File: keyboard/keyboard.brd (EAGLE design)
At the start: 113 x 131.5 mm, 39 parts, among them SW1 CHERRY_MX, SW10 CHERRY_MX, SW11 CHERRY_MX, SW12 CHERRY_MX, SW13 CHERRY_MX, SW14 CHERRY_MX, SW15 CHERRY_MX, SW16 CHERRY_MX, SW17 CHERRY_MX, SW18 CHERRY_MX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

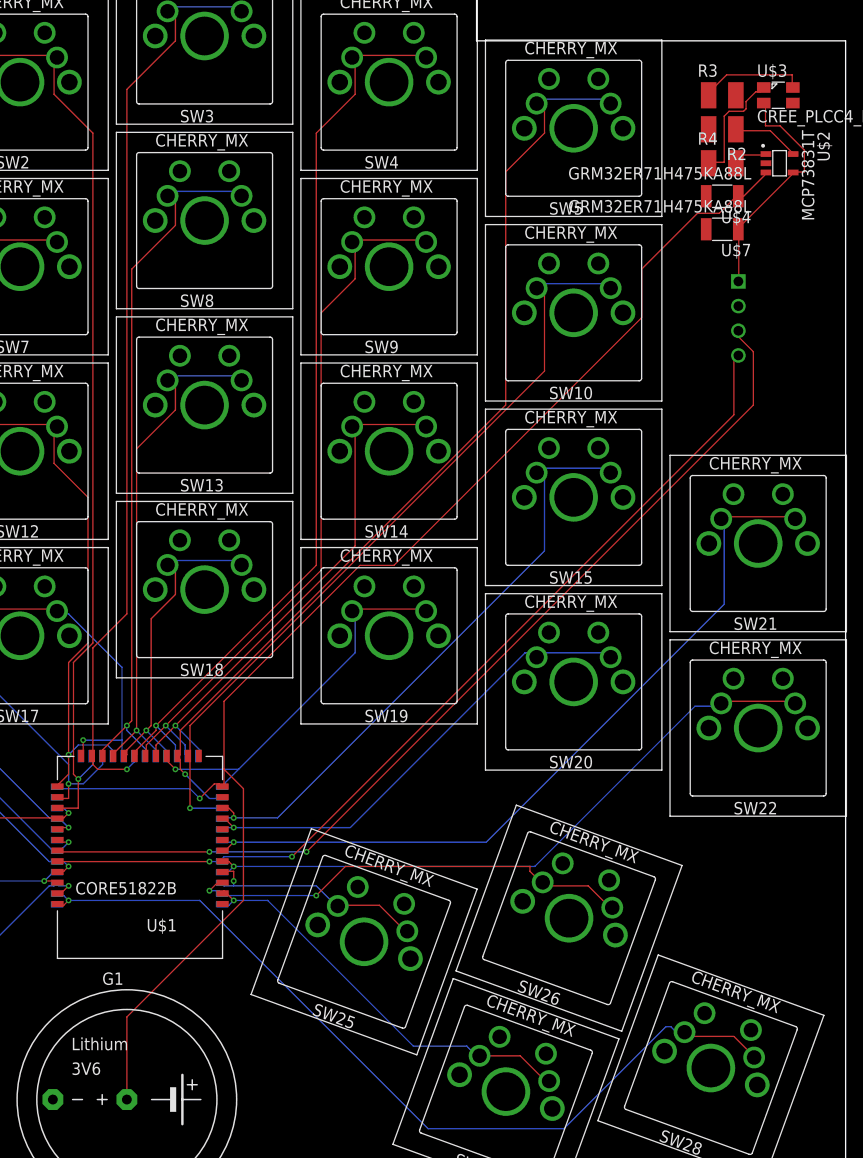
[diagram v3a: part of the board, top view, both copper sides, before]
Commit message: mirror charging circuit on board bottom
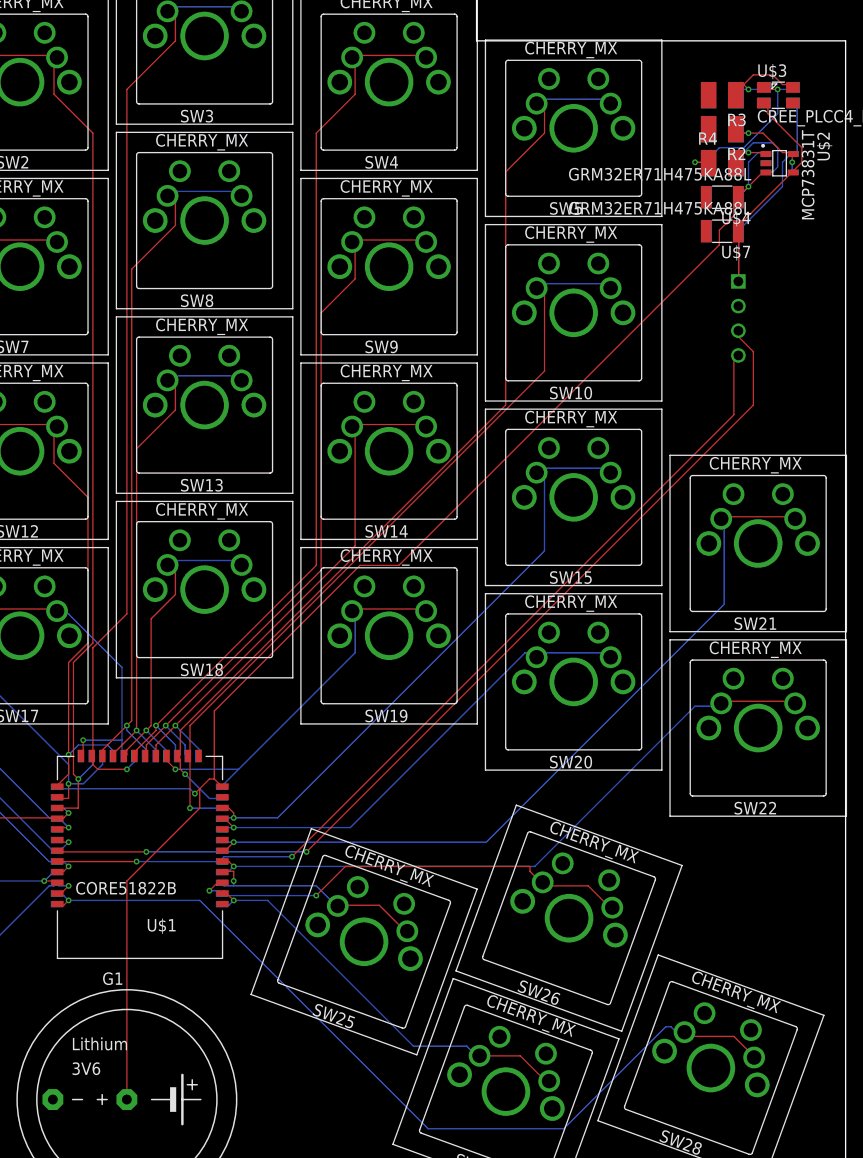
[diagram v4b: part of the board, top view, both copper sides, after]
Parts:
- added R1, R5, R6: 2k, resistor:R1210
- added U$10, U$11: GRM32ER71H475KA88L, GRM32ER71H475KA88L:GRM32ER71H475KA88L
- added U$8: CREE_PLCC4_RGB_LED, cree_plcc4_rgb_led:4-PLCC
- added U$9: MCP73831T, mcp73831t:MCP73831T
- moved U$7 0.20 mm to (100.3, 102.4)
- moved U$4 0.10 mm to (100.3, 105.9)
- turned R3 to 180 degrees
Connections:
- net GND: now also R1.2, R5.2, U$10.P$2, U$11.P$2, U$9.2-VSS
- net GREEN: now also R5.1, U$8.GREEN
- net PROG: now also R1.1, U$9.5-PROG
- net RED: now also R6.1, U$8.RED
- net RSINK: now also R6.2, U$9.1-STAT
- net VCC: now also U$10.P$1, U$9.3-VBAT
- net VIN: now also U$11.P$1, U$8.ANODE, U$9.4VDD
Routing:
- net VIN: track 24.4 -> 45.1 mm
- net RSINK: track 3.53 -> 13.6 mm, vias 0 -> 1
- net RED: track 12.2 -> 18.1 mm, vias 0 -> 2
- net PROG: track 7.02 -> 10.6 mm, vias 0 -> 2
- net GREEN: track 11.1 -> 12.1 mm, vias 0 -> 1
- net VCC: vias 1 -> 2

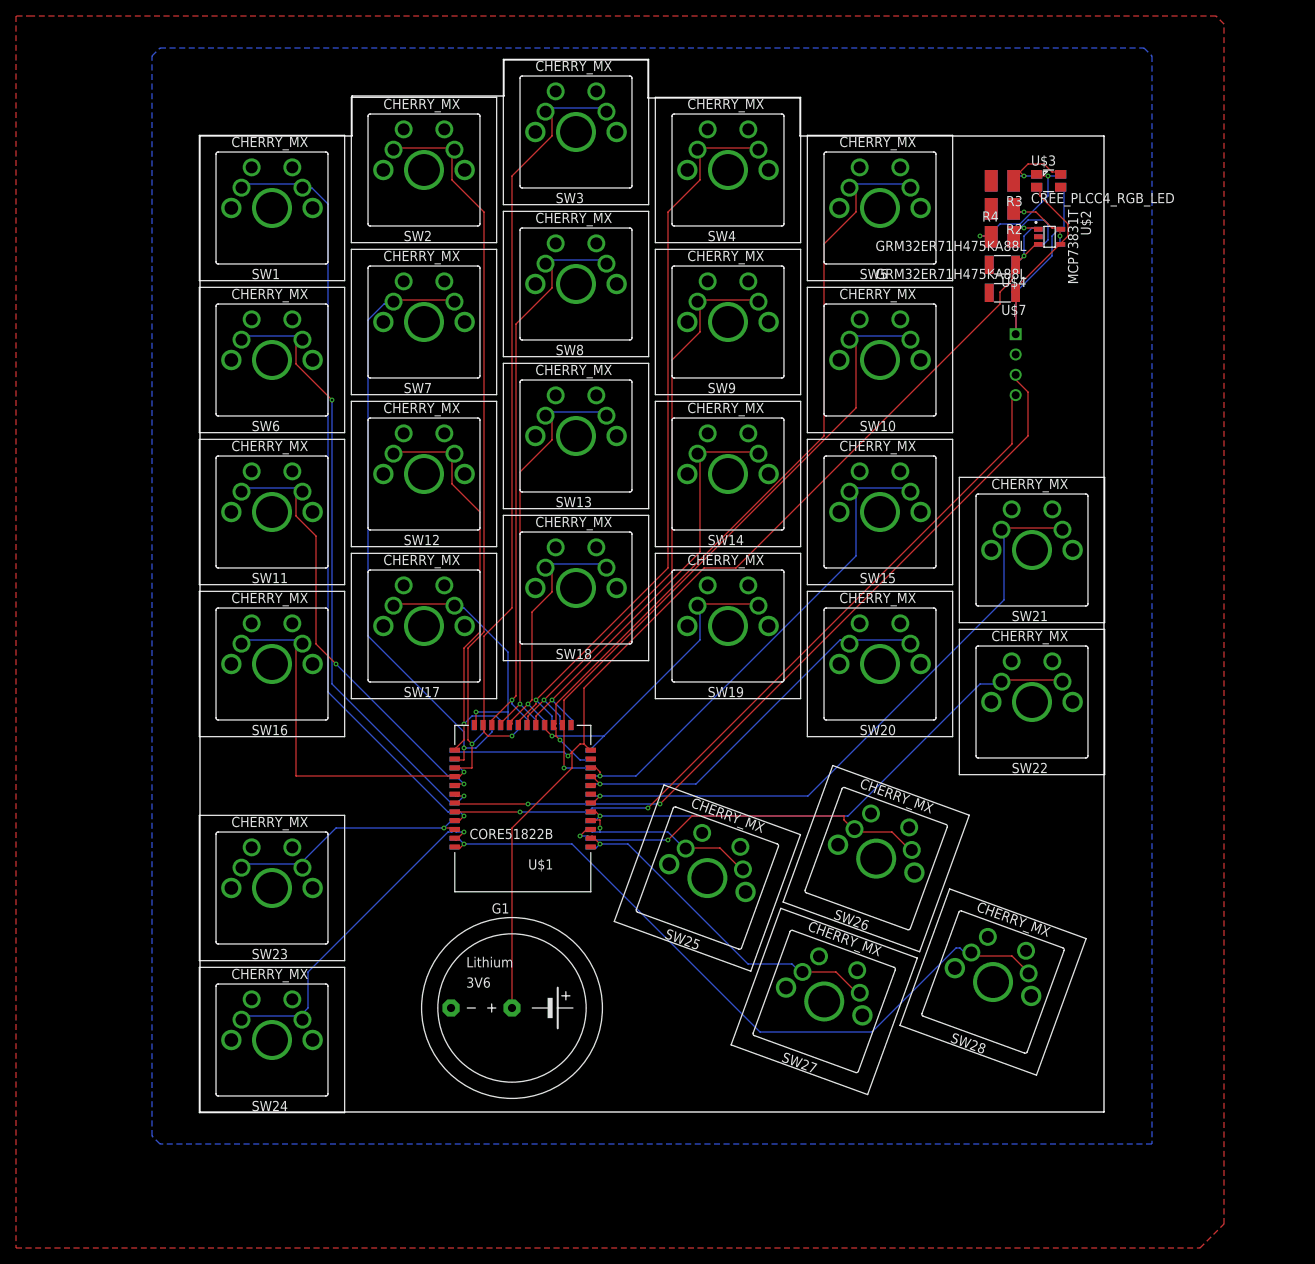
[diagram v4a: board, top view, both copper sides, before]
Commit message: smash labels and values
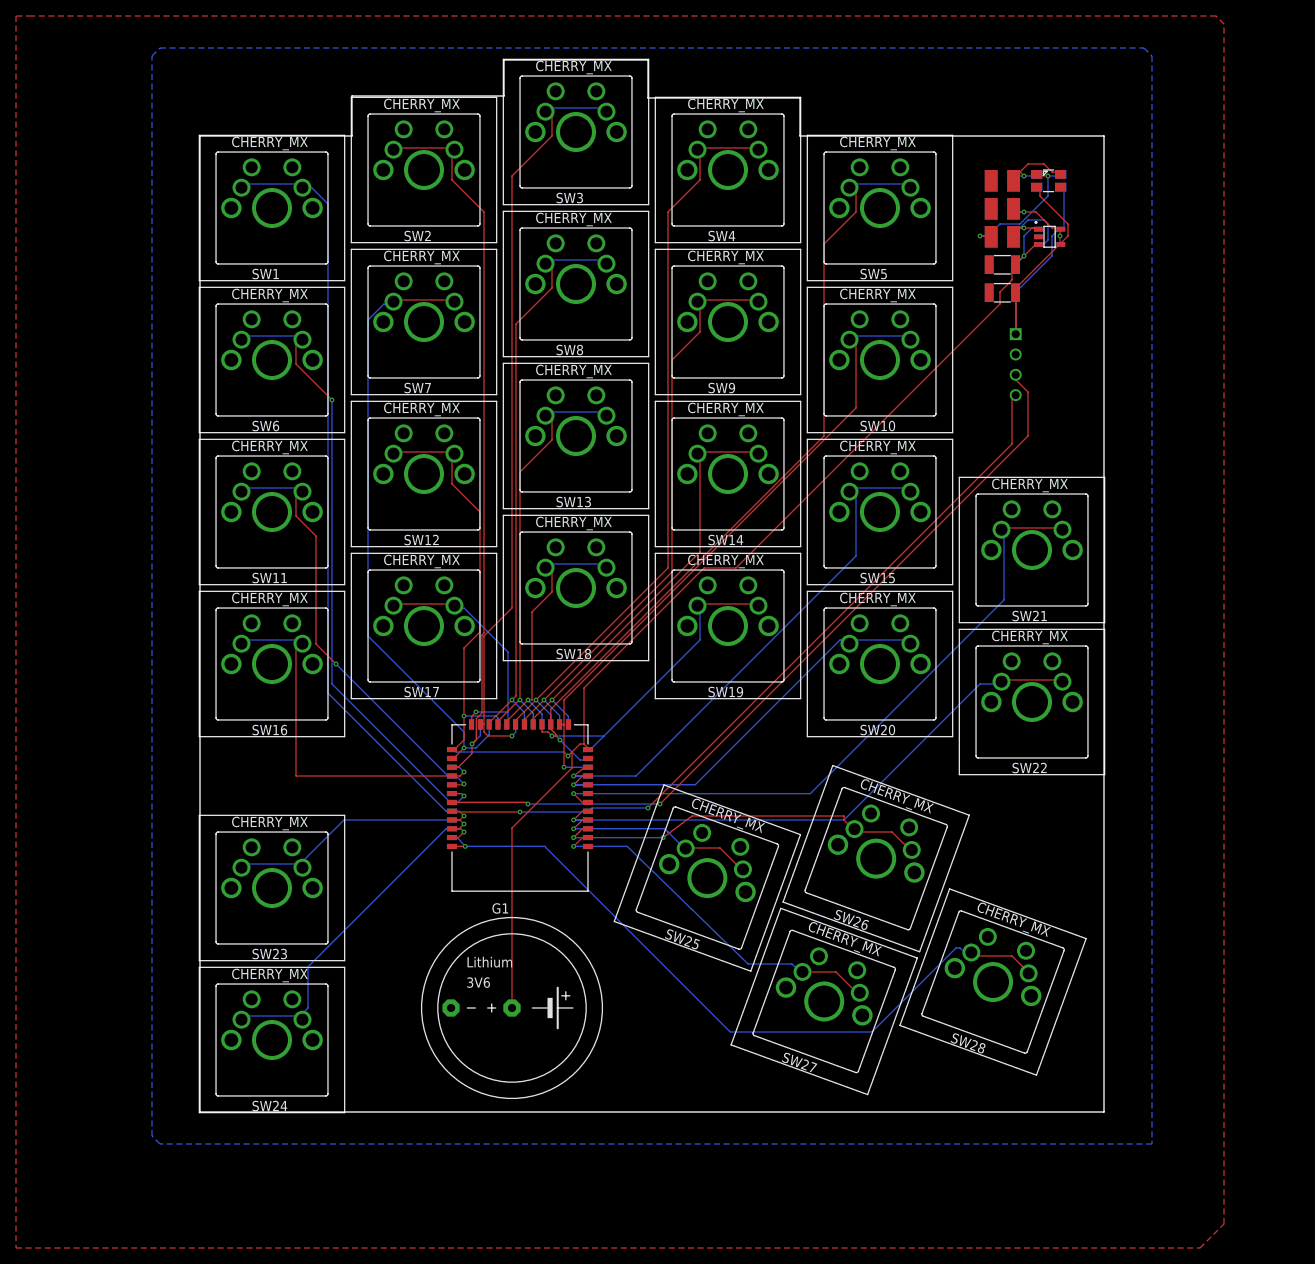
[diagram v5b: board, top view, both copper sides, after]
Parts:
- moved U$1 0.36 mm to (40.0, 38.0)
- moved U$6 0.32 mm to (40.0, 38.0)
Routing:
- net SW20: track 49.9 -> 55.0 mm
- net SW22: track 67.7 -> 72.5 mm
- net SW15: track 63.1 -> 67.8 mm
- net SW21: track 80.2 -> 83.3 mm
- net SW27: track 43.3 -> 45.5 mm
- net SW23: track 31.1 -> 32.9 mm
- net SW25: track 23.8 -> 25.6 mm
- net SW2: track 93.0 -> 91.7 mm
- net SW26: track 46.8 -> 47.8 mm
- net SW18: track 34.0 -> 34.8 mm
- net SW19: track 39.9 -> 40.7 mm
- net SW7: track 78.3 -> 77.6 mm
- net SW28: track 89.5 -> 90.1 mm
- net SWDIO: track 99.1 -> 99.7 mm
- net SW13: track 53.5 -> 54.0 mm
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
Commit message: reroute
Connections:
- new net SW29: U$1.P10, U$6.P30
- net SW10: now also U$1.P30, U$6.P10; no longer U$1.P00, U$6.P13
- net SW12: now also U$6.P13; no longer U$6.P02
- net SW13: now also U$1.P06, U$6.P03; no longer U$1.P07, U$6.P06
- net SW14: now also U$1.P02, U$6.P07; no longer U$1.P03, U$6.P10
- net SW17: now also U$1.P09, U$6.P00; no longer U$1.P10, U$6.P03
- net SW18: now also U$1.P05, U$6.P04; no longer U$1.P06, U$6.P07
- net SW19: now also U$1.P01, U$6.P08; no longer U$1.P02, U$6.P11
- net SW2: now also U$6.P11; no longer U$6.P00
- net SW3: now also U$1.P08, U$6.P01; no longer U$1.P09, U$6.P04
- net SW4: now also U$1.P04, U$6.P05; no longer U$1.P05, U$6.P08
- net SW5: now also U$1.P00, U$6.P09; no longer U$1.P01, U$6.P12
- net SW7: now also U$6.P12; no longer U$6.P01
- net SW8: now also U$1.P07, U$6.P02; no longer U$1.P08, U$6.P05
- net SW9: now also U$1.P03, U$6.P06; no longer U$1.P04, U$6.P09
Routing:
- net SWDIO: track 99.7 -> 214.6 mm, vias 2 -> 3
- net VCC: track 148.3 -> 243.2 mm
- net SW10: track 80.7 -> 128.9 mm, vias 1 -> 2
- net SW15: track 67.8 -> 108.1 mm
- net SW2: track 91.7 -> 114.5 mm
- net PROG: track 10.6 -> 32.9 mm, vias 2 -> 1
- net SW20: track 55.0 -> 76.3 mm
- net SW12: track 53.9 -> 73.3 mm
- net SW11: track 56.0 -> 72.7 mm, vias 2 -> 1
- net SW1: track 98.3 -> 114.1 mm, vias 1 -> 2
- net SW6: track 78.4 -> 93.2 mm, vias 2 -> 1
- net SW7: track 77.6 -> 91.7 mm
- net SW21: track 83.3 -> 96.4 mm
- net SW26: track 47.8 -> 58.6 mm, vias 2 -> 1
- net SW16: track 48.1 -> 37.4 mm
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
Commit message: add induction charger header
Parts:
- added U$12: BATT_HEADER, batt_header:BATT_HEADER
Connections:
- net GND: now also U$12.-
- net VIN: now also U$12.+
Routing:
- net VIN: track 37.9 -> 40.1 mm
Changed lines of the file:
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@@
 <element name="U$10" library="GRM32ER71H475KA88L" package="GRM32ER71H475KA88L" value="GRM32ER71H475KA88L" x="100.3" y="105.9" smashed="yes" rot="MR0"/>
 <element name="U$11" library="GRM32ER71H475KA88L" package="GRM32ER71H475KA88L" value="GRM32ER71H475KA88L" x="100.3" y="102.4" smashed="yes" rot="MR0"/>
+<element name="U$12" library="batt_header" package="BATT_HEADER" value="BATT_HEADER" x="104.17" y="95.975" rot="R270"/>
 </elements>
 <signals>
@@
 <via x="33.22" y="33.22" extent="1-16" drill="0.35"/>
 <wire x1="31.5" y1="33.2" x2="33.22" y2="33.22" width="0.1524" layer="16"/>
+<contactref element="U$12" pad="-"/>
 </signal>
 <signal name="SW1">
@@
 <wire x1="102" y1="102" x2="101.95" y2="102.4" width="0.127" layer="1"/>
 <via x="108" y="113" extent="1-16" drill="0.3048"/>
+<contactref element="U$12" pad="+"/>
+<wire x1="101.96" y1="97.23" x2="104.17" y2="97.245" width="0.1524" layer="1"/>
 </signal>
 <signal name="PROG">

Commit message: finish routing
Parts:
- removed G1: SL-340/P3.6V, battery:SL-340/P3.6V
- added U$13: BATT_HEADER, batt_header:BATT_HEADER
- moved U$2 12.5 mm to (99.8, 98.7), turned to 90 degrees
- moved U$9 12.5 mm to (99.8, 98.7), turned to 270 degrees
- moved U$11 11.1 mm to (98.3, 91.5)
- moved U$7 11.1 mm to (98.3, 91.5)
- moved U$5 8.97 mm to (106.6, 89.5)
- moved U$12 6.14 mm to (98.3, 94.2), turned to 180 degrees
- moved R3 2.33 mm to (98.3, 117.6)
- moved R5 2.33 mm to (98.3, 117.6)
- moved R1 2.28 mm to (98.3, 114.0)
- moved R2 2.28 mm to (98.3, 114.0)
- moved R4 2.24 mm to (98.3, 110.4)
- moved R6 2.24 mm to (98.3, 110.4)
- moved U$10 2.15 mm to (98.3, 106.7)
- moved U$4 2.15 mm to (98.3, 106.7)
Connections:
- net GND: now also U$13.-; no longer G1.-
- net VCC: now also U$13.+; no longer G1.+
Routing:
- net VCC: track 243.2 -> 139.2 mm
- net SWCLK: track 105.8 -> 175.6 mm, vias 3 -> 2
- net SWDIO: track 214.6 -> 182.4 mm, vias 3 -> 1
- net VIN: track 40.1 -> 63.2 mm
- net RSINK: track 8.47 -> 28.7 mm
- net PROG: track 32.9 -> 22.9 mm, vias 1 -> 2
- net GREEN: track 11.8 -> 16.5 mm
- net RED: track 18.1 -> 18.7 mm
- net GND: vias 2 -> 4
